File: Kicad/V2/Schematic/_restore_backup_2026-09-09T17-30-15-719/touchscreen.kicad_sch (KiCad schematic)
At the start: 1 part

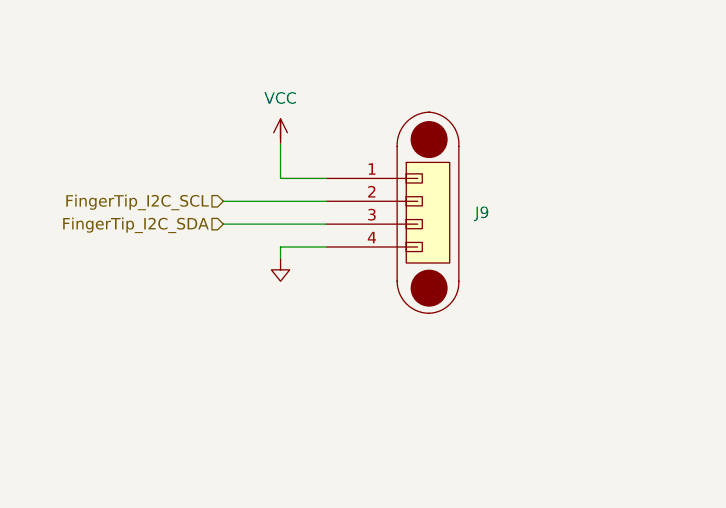
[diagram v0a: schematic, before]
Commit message: finition schematic de reference
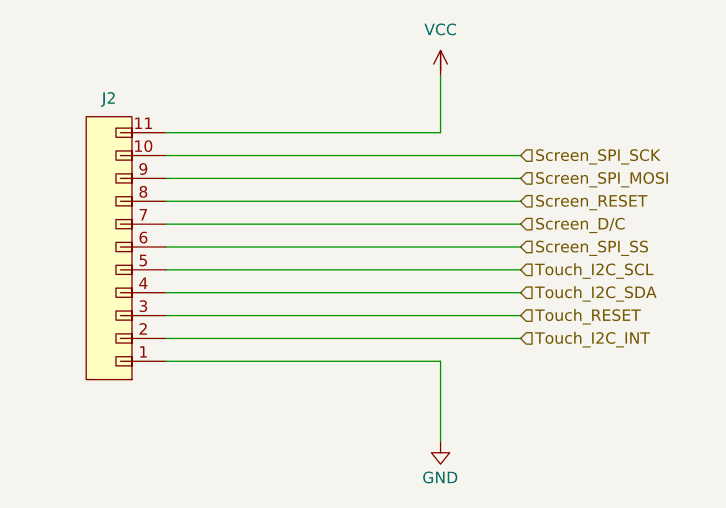
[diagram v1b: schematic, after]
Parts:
- removed J9: (no value), MyGlove:PinHeader_1x04_P2.54mm_Vertical, symbol G-Love:Conn_POGO_4
- added J2: (no value), MyGlove:PinHeader_1x11_P2.54mm_Vertical, symbol G-Love:Conn_11_pins
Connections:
- net GND: now also J2.1
- net VCC: now also J2.11
- new net Screen_D/C: J2.7
- new net Screen_RESET: J2.8
- new net Screen_SPI_MOSI: J2.9
- new net Screen_SPI_SCK: J2.10
- new net Screen_SPI_SS: J2.6
- new net Touch_I2C_INT: J2.2
- new net Touch_I2C_SCL: J2.5
- new net Touch_I2C_SDA: J2.4
- new net Touch_RESET: J2.3
